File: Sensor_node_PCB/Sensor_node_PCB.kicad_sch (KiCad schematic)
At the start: 21 parts, among them J1 Conn_02x14_Counter_Clockwise, Q1 NMOS, Q2 NMOS, Q3 NMOS, U1 INA219AxD

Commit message: Node pcb schematic update
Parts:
- removed C1, C2, C3: 1u, symbol Device:C
- added C1, C2, C3: 1u, symbol Device:C_Polarized
- added C4, C5, C6: 0.1u, symbol Device:C
- added C7: 10u, symbol Device:C_Polarized
- added J2: Logic power, symbol Connector_Generic:Conn_01x02
- added R13: 10k, symbol Device:R
- added R14: R, symbol Device:R
- J1: value Conn_02x14_Counter_Clockwise -> DIP28_socket; footprint (none) -> Package_DIP:DIP-28_W7.62mm_Socket
- R2: value 9.4 -> 4.7
- R3: value 18.8 -> 10
- R4: value 37.6 -> 22
- R7, R8, R9: value 150 -> 160
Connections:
- net GND: now also J1.19 (Pin_19), J1.27 (Pin_27), J1.8 (Pin_8), C1.2, C2.2, C3.2, C4.2, C5.2, C6.2, C7.2, J2.2 (Pin_2)
- net PWM1: now also J1.16 (Pin_16)
- net PWM2: now also J1.15 (Pin_15)
- net PWM3: now also J1.14 (Pin_14)
- net at J1.1 (Pin_1): now also R14.1
- net at J1.13 (Pin_13): now also C5.1
- net SCL: now reaches J1.17 (Pin_17)
- net SCL: now also R6.2, U1.4 (SCL)
- net SDA: now reaches J1.18 (Pin_18)
- net SDA: now also R5.2, U1.3 (SDA)
- net MOSI: now reaches J1.2 (Pin_2)
- net at J1.20 (Pin_20): now also C7.1
- net at J1.28 (Pin_28): now also C4.1
- net CLK: now reaches J1.3 (Pin_3)
- net MISO: now reaches J1.6 (Pin_6)
- net CS: now reaches J1.7 (Pin_7)
- net at Q2.2 (G), R11.1, R8.1: now also C2.1
- net at Q3.2 (G), R12.1, R9.1: now also C3.1
- net at Q1.2 (G), R10.1, R7.1: now also C1.1
- new net: C6.1, R13.2, R14.2
- new net VDD: J2.1 (Pin_1), R13.1
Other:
- note added: "adicionar leds indicadores"
- note added: "confirmar footprint do pic"
- note added: "confirmar pinos do SPI"
- note removed: "Estes valores das resistências são os ideais (R2, R3, R4). Na realidade como andamos a juntar várias resistências são ligeiramente diferentes."
- moved on the sheet: J1

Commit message: PCB schematic updates
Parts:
- added J3: Programmer, Connector_PinHeader_2.54mm:PinHeader_1x06_P2.54mm_Vertical, symbol Connector:Conn_01x06_Pin
- R14: value R -> 100
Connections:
- net GND: now also J3.3 (Pin_3)
- net VDD: now also J3.2 (Pin_2)
- net MCLR: now reaches J1.1 (Pin_1), R14.1
- net MCLR: now also J3.1 (Pin_1)
- net LED2: now reaches J1.10 (Pin_10)
- net LED3: now reaches J1.12 (Pin_12)
- net PGD2: now reaches J1.21 (Pin_21)
- net PGD2: now also J3.4 (Pin_4)
- net PGC2: now reaches J1.22 (Pin_22)
- net PGC2: now also J3.5 (Pin_5)
- net LED1: now reaches J1.9 (Pin_9)
- no-connect marks 0 -> 1
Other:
- note added: "por label silkscreen qual o pino 1 (seta do pickit)"
- note removed: "confirmar footprint do pic"
- moved on the sheet: R14

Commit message: PCB layout started
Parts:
- removed R1: 100m, symbol Device:R_Shunt
- added C8: 0.1u, Capacitor_THT:C_Rect_L7.0mm_W3.5mm_P5.00mm, symbol Device:C
- added D1, D2, D3: LED, LED_THT:LED_D4.0mm, symbol Device:LED
- added J4: SPI breakout, Connector_PinHeader_2.54mm:PinHeader_1x04_P2.54mm_Vertical, symbol Connector:Conn_01x04_Pin
- added R1: 100m, Resistor_THT:R_Axial_DIN0309_L9.0mm_D3.2mm_P12.70mm_Horizontal, symbol Device:R
- added R15, R16, R17: R, Resistor_THT:R_Axial_DIN0309_L9.0mm_D3.2mm_P12.70mm_Horizontal, symbol Device:R
- BT1: footprint (none) -> Connector_PinHeader_1.00mm:PinHeader_1x02_P1.00mm_Vertical
- C1, C2, C3, C7: footprint (none) -> Capacitor_THT:CP_Radial_D5.0mm_P2.00mm
- C4, C5, C6: footprint (none) -> Capacitor_THT:C_Rect_L7.0mm_W3.5mm_P5.00mm
- J2: footprint (none) -> Connector_PinHeader_2.54mm:PinHeader_1x02_P2.54mm_Vertical
- Q1, Q2, Q3: footprint (none) -> Package_TO_SOT_THT:TO-220-3_Vertical
- R10, R11, R12, R13, R14, R5, R6, R7, R8, R9: footprint (none) -> Resistor_THT:R_Axial_DIN0309_L9.0mm_D3.2mm_P12.70mm_Horizontal
- R2: footprint (none) -> Resistor_THT:R_Axial_Power_L38.0mm_W9.0mm_P45.72mm
- R3, R4: footprint (none) -> Resistor_THT:R_Axial_Power_L50.0mm_W9.0mm_P55.88mm
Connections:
- net 3V3 is gone; now on net VDD: R5.1, R6.1, U1.5 (VS)
- net CLK: now also J4.2 (Pin_2)
- net CS: now also J4.4 (Pin_4)
- net GND: now also C8.1, D1.1 (K), D2.1 (K), D3.1 (K)
- net LED1: now also R15.1
- net LED2: now also R16.1
- net LED3: now also R17.1
- net MISO: now also J4.3 (Pin_3)
- net MOSI: now also J4.1 (Pin_1)
- net VDD: now also C8.2
- net at R2.1, R3.1, R4.1: now also U1.7 (IN-), R1.2
- net at U1.8 (IN+): now also BT1.1 (+), R1.1
- new net: D2.2 (A), R16.2
- new net: D1.2 (A), R15.2
- new net: D3.2 (A), R17.2
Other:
- note added: "footprint dos mosfets tem gate e dreno trocados"
- note added: "footprint resistencia shunt"
- note removed: "adicionar leds indicadores"
- moved on the sheet: J2

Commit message: PCB corrections and improvements
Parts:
- Q1, Q2, Q3: footprint Package_TO_SOT_THT:TO-220-3_Vertical -> Package_TO_SOT_THT:TO-220F-3_Horizontal_TabUp
- R1: footprint Resistor_THT:R_Axial_DIN0309_L9.0mm_D3.2mm_P12.70mm_Horizontal -> Capacitor_SMD:C_1206_3216Metric_Pad1.33x1.80mm_HandSolder
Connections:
- net CLK: now also J4.1 (Pin_1); no longer J4.2 (Pin_2)
- net MISO: now also J4.2 (Pin_2); no longer J4.3 (Pin_3)
- net MOSI: now also J4.3 (Pin_3); no longer J4.1 (Pin_1)
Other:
- note removed: "footprint dos mosfets tem gate e dreno trocados"
- note removed: "footprint resistencia shunt"
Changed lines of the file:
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@@
 		)
 	)
-	(text "footprint resistencia shunt"
-		(exclude_from_sim no)
-		(at 72.644 16.256 0)
-		(effects
-			(font
-				(size 1.27 1.27)
-			)
-		)
-	)
-	(text "footprint dos mosfets tem gate e dreno trocados"
-		(exclude_from_sim no)
-		(at 131.826 20.32 0)
-		(effects
-			(font
-				(size 1.27 1.27)
-			)
-		)
-	)
 	(global_label "PGC2"
 		(shape input)
@@
 		)
 	)
+	(global_label "CLK"
+		(shape input)
+		(at 46.99 116.84 0)
+		(fields_autoplaced yes)
+		(effects
+			(font
+				(size 1.27 1.27)
+			)
+			(justify left)
+		)
+		(property "Intersheetrefs" "${INTERSHEET_REFS}"
+			(at 53.5433 116.84 0)
+			(effects
+				(font
+					(size 1.27 1.27)
+				)
+				(justify left)
+				(hide yes)
+			)
+		)
+	)
 	(global_label "PGC2"
 		(shape input)
@@
 		)
 	)
-	(global_label "CLK"
+	(global_label "MOSI"
 		(shape input)
-		(at 115.57 78.74 180)
+		(at 46.99 121.92 0)
 		(fields_autoplaced yes)
 		(effects
@@
 				(size 1.27 1.27)
 			)
-			(justify right)
+			(justify left)
 		)
 		(property "Intersheetrefs" "${INTERSHEET_REFS}"
-			(at 109.0167 78.74 0)
+			(at 54.5714 121.92 0)
 			(effects
 				(font
 					(size 1.27 1.27)
 				)
-				(justify right)
+				(justify left)
 				(hide yes)
 			)
 		)
 	)
-	(global_label "LED1"
+	(global_label "CLK"
 		(shape input)
-		(at 171.45 74.93 180)
+		(at 115.57 78.74 180)
 		(fields_autoplaced yes)
 		(effects
@@
 		)
 		(property "Intersheetrefs" "${INTERSHEET_REFS}"
-			(at 163.8082 74.93 0)
+			(at 109.0167 78.74 0)
 			(effects
 				(font
@@
 		)
 	)
-	(global_label "CS"
+	(global_label "LED1"
 		(shape input)
-		(at 115.57 88.9 180)
+		(at 171.45 74.93 180)
 		(fields_autoplaced yes)
 		(effects
@@
 		)
 		(property "Intersheetrefs" "${INTERSHEET_REFS}"
-			(at 110.1053 88.9 0)
+			(at 163.8082 74.93 0)
 			(effects
 				(font
@@
 		)
 	)
-	(global_label "SDA"
+	(global_label "CS"
 		(shape input)
-		(at 128.27 99.06 0)
+		(at 115.57 88.9 180)
 		(fields_autoplaced yes)
 		(effects
@@
 				(size 1.27 1.27)
 			)
-			(justify left)
+			(justify right)
 		)
 		(property "Intersheetrefs" "${INTERSHEET_REFS}"
-			(at 134.8233 99.06 0)
+			(at 110.1053 88.9 0)
 			(effects
 				(font
 					(size 1.27 1.27)
 				)
-				(justify left)
+				(justify right)
 				(hide yes)
 			)
 		)
 	)
-	(global_label "CLK"
+	(global_label "SDA"
 		(shape input)
-		(at 46.99 119.38 0)
+		(at 128.27 99.06 0)
 		(fields_autoplaced yes)
 		(effects
@@
 		)
 		(property "Intersheetrefs" "${INTERSHEET_REFS}"
-			(at 53.5433 119.38 0)
+			(at 134.8233 99.06 0)
 			(effects
 				(font
@@
 		)
 	)
-	(global_label "MOSI"
-		(shape input)
-		(at 46.99 116.84 0)
-		(fields_autoplaced yes)
-		(effects
-			(font
-				(size 1.27 1.27)
-			)
-			(justify left)
-		)
-		(property "Intersheetrefs" "${INTERSHEET_REFS}"
-			(at 54.5714 116.84 0)
-			(effects
-				(font
-					(size 1.27 1.27)
-				)
-				(justify left)
-				(hide yes)
-			)
-		)
-	)
 	(global_label "LED3"
 		(shape input)
@@
 	(global_label "MISO"
 		(shape input)
-		(at 46.99 121.92 0)
+		(at 46.99 119.38 0)
 		(fields_autoplaced yes)
 		(effects
@@
 		)
 		(property "Intersheetrefs" "${INTERSHEET_REFS}"
-			(at 54.5714 121.92 0)
+			(at 54.5714 119.38 0)
 			(effects
 				(font
@@
 			)
 		)
-		(property "Footprint" "Resistor_THT:R_Axial_DIN0309_L9.0mm_D3.2mm_P12.70mm_Horizontal"
+		(property "Footprint" "Capacitor_SMD:C_1206_3216Metric_Pad1.33x1.80mm_HandSolder"
 			(at 71.12 27.178 90)
 			(effects
@@
 			)
 		)
-		(property "Footprint" "Package_TO_SOT_THT:TO-220-3_Vertical"
+		(property "Footprint" "Package_TO_SOT_THT:TO-220F-3_Horizontal_TabUp"
 			(at 181.61 35.56 0)
 			(effects
@@
 			)
 		)
-		(property "Footprint" "Package_TO_SOT_THT:TO-220-3_Vertical"
+		(property "Footprint" "Package_TO_SOT_THT:TO-220F-3_Horizontal_TabUp"
 			(at 137.16 35.56 0)
 			(effects
@@
 			)
 		)
-		(property "Footprint" "Package_TO_SOT_THT:TO-220-3_Vertical"
+		(property "Footprint" "Package_TO_SOT_THT:TO-220F-3_Horizontal_TabUp"
 			(at 92.71 35.56 0)
 			(effects

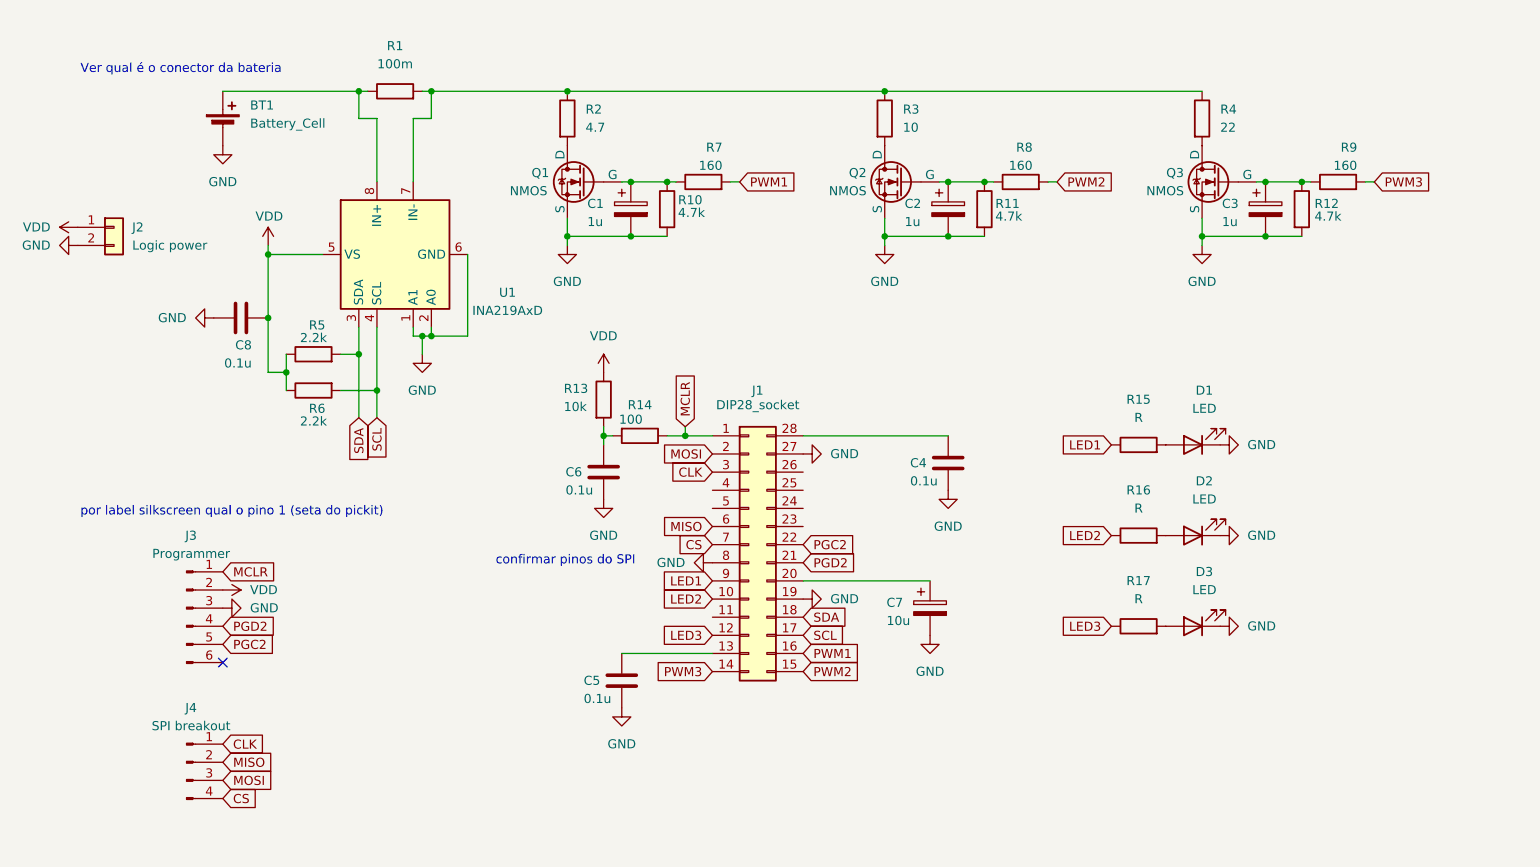
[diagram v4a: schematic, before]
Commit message: PCB layout redone as shield for devboard
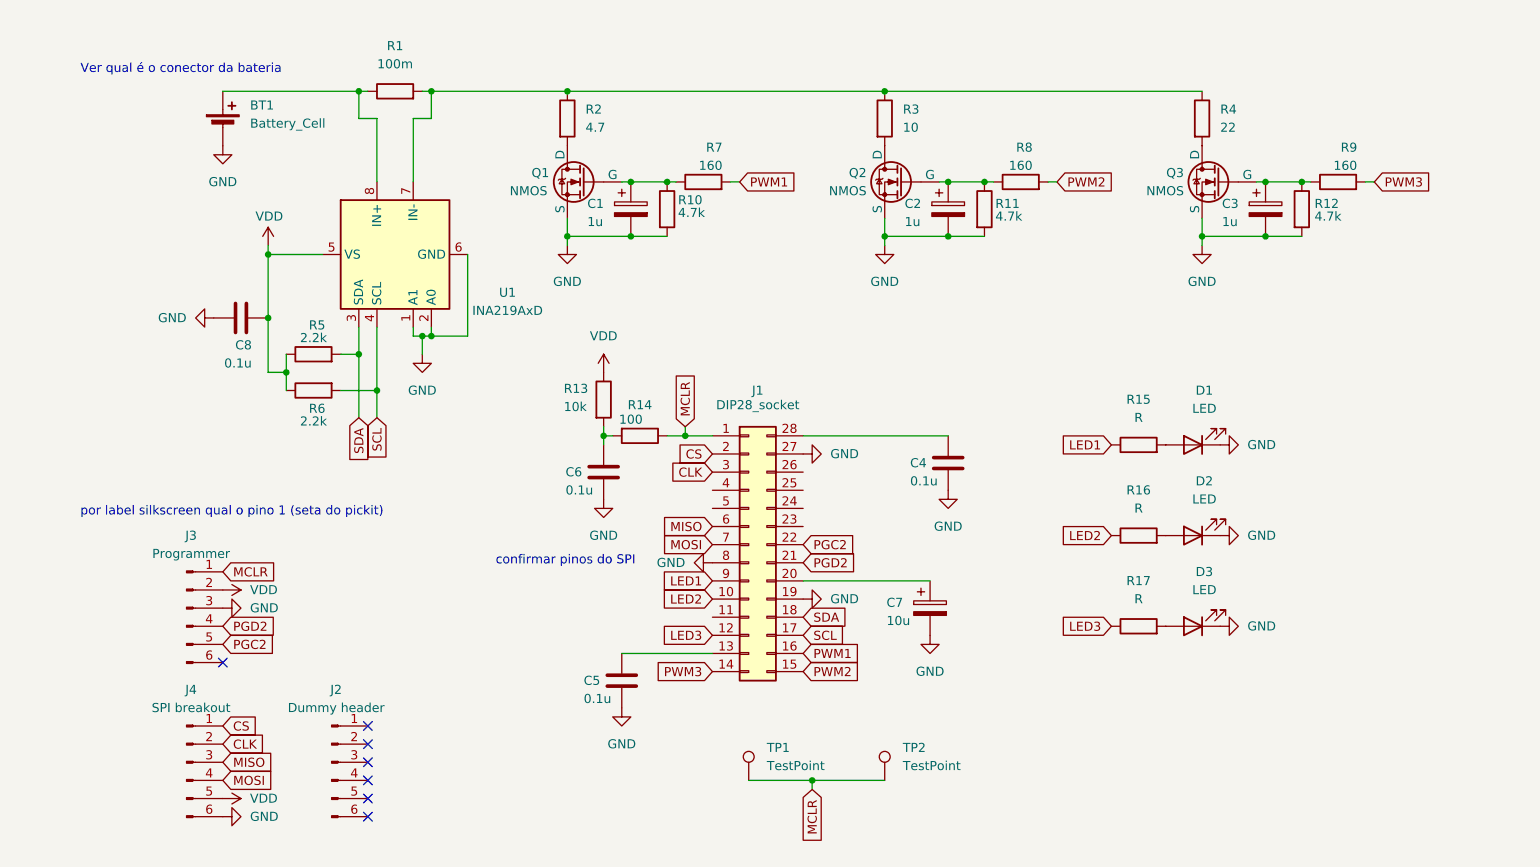
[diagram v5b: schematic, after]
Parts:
- removed J2: Logic power, Connector_PinHeader_2.54mm:PinHeader_1x02_P2.54mm_Vertical, symbol Connector_Generic:Conn_01x02
- added J2: Dummy header, Connector_PinHeader_2.54mm:PinHeader_1x06_P2.54mm_Vertical, symbol Connector:Conn_01x06_Pin
- added TP1, TP2: TestPoint, TestPoint:TestPoint_THTPad_1.5x1.5mm_Drill0.7mm, symbol Connector:TestPoint
- J4: footprint Connector_PinHeader_2.54mm:PinHeader_1x04_P2.54mm_Vertical -> Connector_PinHeader_2.54mm:PinHeader_1x06_P2.54mm_Vertical; symbol Connector:Conn_01x04_Pin -> Connector:Conn_01x06_Pin
- Q1, Q2, Q3: footprint Package_TO_SOT_THT:TO-220F-3_Horizontal_TabUp -> Package_TO_SOT_THT:TO-220-3_Vertical
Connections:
- net CLK: now also J4.2 (Pin_2); no longer J4.1 (Pin_1)
- net CS: now also J1.2 (Pin_2), J4.1 (Pin_1); no longer J1.7 (Pin_7), J4.4 (Pin_4)
- net GND: now also J4.6 (Pin_6)
- net MCLR: now also TP1.1, TP2.1
- net MISO: now also J4.3 (Pin_3); no longer J4.2 (Pin_2)
- net MOSI: now also J1.7 (Pin_7), J4.4 (Pin_4); no longer J1.2 (Pin_2), J4.3 (Pin_3)
- net VDD: now also J4.5 (Pin_5)
- no-connect marks 1 -> 7

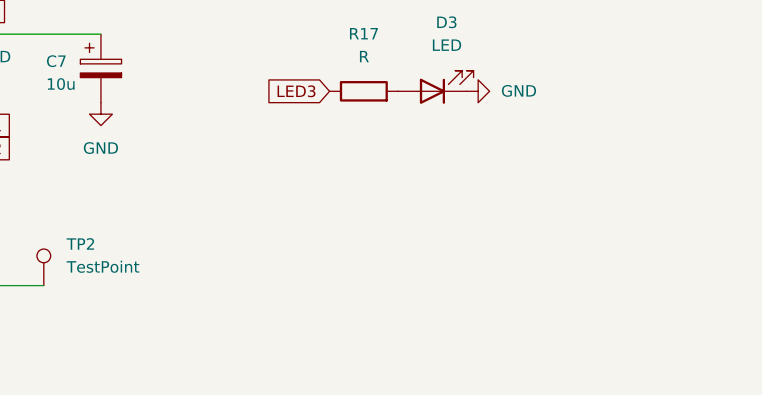
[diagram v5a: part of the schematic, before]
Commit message: PCB redone according to fabrication specs
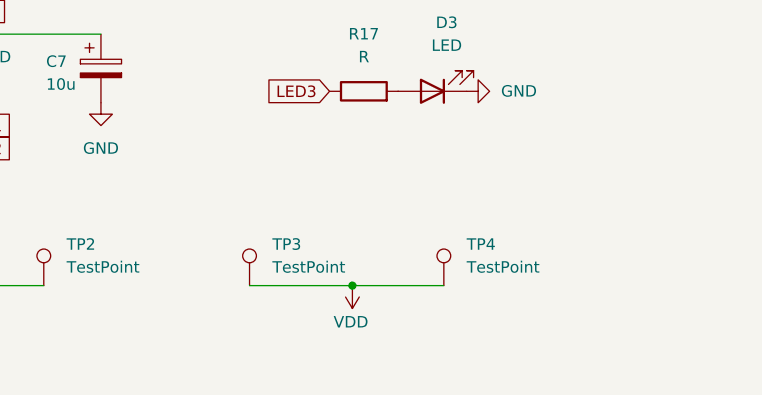
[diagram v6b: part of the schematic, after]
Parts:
- added TP3, TP4: TestPoint, TestPoint:TestPoint_THTPad_1.5x1.5mm_Drill0.7mm, symbol Connector:TestPoint
- BT1: footprint Connector_PinHeader_1.00mm:PinHeader_1x02_P1.00mm_Vertical -> Connector_PinHeader_2.00mm:PinHeader_1x02_P2.00mm_Vertical
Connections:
- net VDD: now also TP3.1, TP4.1
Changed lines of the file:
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@@
 	)
 	(junction
+		(at 173.99 121.92)
+		(diameter 0)
+		(color 0 0 0 0)
+	)
+	(junction
 		(at 53.34 48.26)
 		(diameter 0)
@@
 	(wire
 		(pts
+			(xy 173.99 121.92) (xy 184.15 121.92)
+		)
+		(stroke
+			(width 0)
+			(type default)
+		)
+	)
+	(wire
+		(pts
 			(xy 66.04 62.23) (xy 66.04 71.12)
 		)
@@
 	(wire
 		(pts
+			(xy 162.56 121.92) (xy 173.99 121.92)
+		)
+		(stroke
+			(width 0)
+			(type default)
+		)
+	)
+	(wire
+		(pts
 			(xy 68.58 67.31) (xy 68.58 71.12)
 		)
@@
 	)
 	(symbol
+		(lib_id "power:VDD")
+		(at 173.99 121.92 180)
+		(unit 1)
+		(exclude_from_sim no)
+		(in_bom yes)
+		(on_board yes)
+		(dnp no)
+		(property "Reference" "#PWR015"
+			(at 173.99 118.11 0)
+			(effects
+				(font
+					(size 1.27 1.27)
+				)
+				(hide yes)
+			)
+		)
+		(property "Value" "VDD"
+			(at 175.768 125.984 0)
+			(effects
+				(font
+					(size 1.27 1.27)
+				)
+				(justify left)
+			)
+		)
+		(property "Footprint" ""
+			(at 173.99 121.92 0)
+			(effects
+				(font
+					(size 1.27 1.27)
+				)
+				(hide yes)
+			)
+		)
+		(property "Datasheet" ""
+			(at 173.99 121.92 0)
+			(effects
+				(font
+					(size 1.27 1.27)
+				)
+				(hide yes)
+			)
+		)
+		(property "Description" "Power symbol creates a global label with name \"VDD\""
+			(at 173.99 121.92 0)
+			(effects
+				(font
+					(size 1.27 1.27)
+				)
+				(hide yes)
+			)
+		)
+		(pin "1"
+		)
+		(instances
+			(project "Sensor_node_PCB"
+				(path "/c9ef9ad9-c769-4c3b-ad3d-4e0c492bcfd2"
+					(reference "#PWR015")
+					(unit 1)
+				)
+			)
+		)
+	)
+	(symbol
 		(lib_id "Device:R")
 		(at 175.26 74.93 90)
@@
 	)
 	(symbol
+		(lib_id "Connector:TestPoint")
+		(at 184.15 121.92 0)
+		(unit 1)
+		(exclude_from_sim no)
+		(in_bom yes)
+		(on_board yes)
+		(dnp no)
+		(fields_autoplaced yes)
+		(property "Reference" "TP4"
+			(at 186.69 117.3479 0)
+			(effects
+				(font
+					(size 1.27 1.27)
+				)
+				(justify left)
+			)
+		)
+		(property "Value" "TestPoint"
+			(at 186.69 119.8879 0)
+			(effects
+				(font
+					(size 1.27 1.27)
+				)
+				(justify left)
+			)
+		)
+		(property "Footprint" "TestPoint:TestPoint_THTPad_1.5x1.5mm_Drill0.7mm"
+			(at 189.23 121.92 0)
+			(effects
+				(font
+					(size 1.27 1.27)
+				)
+				(hide yes)
+			)
+		)
+		(property "Datasheet" "~"
+			(at 189.23 121.92 0)
+			(effects
+				(font
+					(size 1.27 1.27)
+				)
+				(hide yes)
+			)
+		)
+		(property "Description" "test point"
+			(at 184.15 121.92 0)
+			(effects
+				(font
+					(size 1.27 1.27)
+				)
+				(hide yes)
+			)
+		)
+		(property "Mouser link" ""
+			(at 184.15 121.92 0)
+			(effects
+				(font
+					(size 1.27 1.27)
+				)
+				(hide yes)
+			)
+		)
+		(pin "1"
+		)
+		(instances
+			(project "Sensor_node_PCB"
+				(path "/c9ef9ad9-c769-4c3b-ad3d-4e0c492bcfd2"
+					(reference "TP4")
+					(unit 1)
+				)
+			)
+		)
+	)
+	(symbol
 		(lib_id "Device:LED")
 		(at 182.88 74.93 180)
@@
 	)
 	(symbol
+		(lib_id "Connector:TestPoint")
+		(at 162.56 121.92 0)
+		(unit 1)
+		(exclude_from_sim no)
+		(in_bom yes)
+		(on_board yes)
+		(dnp no)
+		(fields_autoplaced yes)
+		(property "Reference" "TP3"
+			(at 165.1 117.3479 0)
+			(effects
+				(font
+					(size 1.27 1.27)
+				)
+				(justify left)
+			)
+		)
+		(property "Value" "TestPoint"
+			(at 165.1 119.8879 0)
+			(effects
+				(font
+					(size 1.27 1.27)
+				)
+				(justify left)
+			)
+		)
+		(property "Footprint" "TestPoint:TestPoint_THTPad_1.5x1.5mm_Drill0.7mm"
+			(at 167.64 121.92 0)
+			(effects
+				(font
+					(size 1.27 1.27)
+				)
+				(hide yes)
+			)
+		)
+		(property "Datasheet" "~"
+			(at 167.64 121.92 0)
+			(effects
+				(font
+					(size 1.27 1.27)
+				)
+				(hide yes)
+			)
+		)
+		(property "Description" "test point"
+			(at 162.56 121.92 0)
+			(effects
+				(font
+					(size 1.27 1.27)
+				)
+				(hide yes)
+			)
+		)
+		(property "Mouser link" ""
+			(at 162.56 121.92 0)
+			(effects
+				(font
+					(size 1.27 1.27)
+				)
+				(hide yes)
+			)
+		)
+		(pin "1"
+		)
+		(instances
+			(project "Sensor_node_PCB"
+				(path "/c9ef9ad9-c769-4c3b-ad3d-4e0c492bcfd2"
+					(reference "TP3")
+					(unit 1)
+				)
+			)
+		)
+	)
+	(symbol
 		(lib_id "Device:C_Polarized")
 		(at 104.14 41.91 0)
@@
 			)
 		)
-		(property "Footprint" "Connector_PinHeader_1.00mm:PinHeader_1x02_P1.00mm_Vertical"
+		(property "Footprint" "Connector_PinHeader_2.00mm:PinHeader_1x02_P2.00mm_Vertical"
 			(at 46.99 28.956 90)
 			(effects
